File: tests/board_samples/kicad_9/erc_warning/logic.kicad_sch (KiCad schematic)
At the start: 5 parts, among them U1 74LS04, U2 74AHC1G126, U4 74AHC1G126

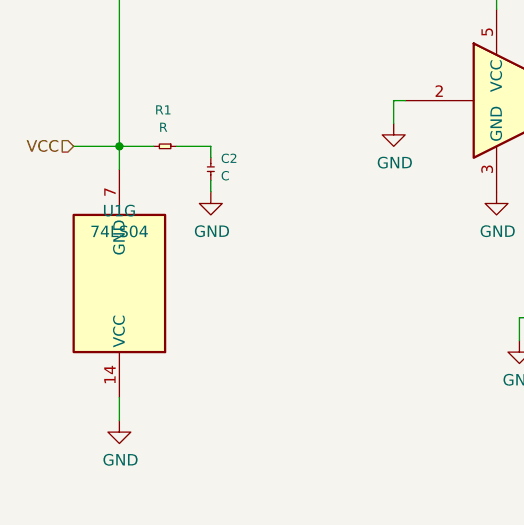
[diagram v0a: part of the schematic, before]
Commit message: [Tests][Fixed] The ERC warning case
- GND wrongly connected
- Catched by the new `ground_pin_not_ground` check from KiCad 10
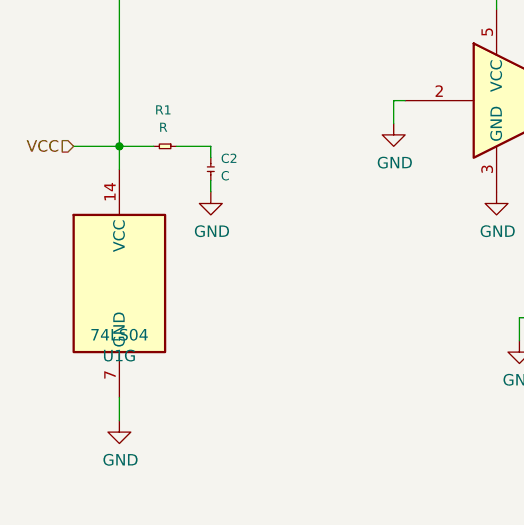
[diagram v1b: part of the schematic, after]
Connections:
- net GND: now also U1.7 (GND); no longer U1.14 (VCC)
- net VCC: now also U1.14 (VCC); no longer U1.7 (GND)
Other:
- moved on the sheet: U1G
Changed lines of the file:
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@@
 (kicad_sch
-	(version 20241209)
+	(version 20250114)
 	(generator "eeschema")
 	(generator_version "9.0")
@@
 	(symbol
 		(lib_id "74xx:74LS04")
-		(at 107.95 78.74 180)
+		(at 107.95 78.74 0)
 		(unit 7)
 		(exclude_from_sim no)
@@
 		(dnp no)
 		(property "Reference" "U1"
-			(at 107.95 70.6882 0)
+			(at 107.95 86.7918 0)
 			(effects
 				(font
@@
 		)
 		(property "Value" "74LS04"
-			(at 107.95 72.9996 0)
-			(effects
-				(font
+			(at 107.95 84.4804 0)
+			(effects
+				(font
